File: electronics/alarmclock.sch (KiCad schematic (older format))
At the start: 31 parts, among them J1 Conn_01x02, J2 SWD, J3 SocketTop, J4 SocketBottom, J5 Conn_01x02, Q1 Backpower, SW1 Rotary_Encoder_Switch, SW2 Reset, U1 STM32L031F6P6, U2 74HC595, U3 74HC595, U4 AP2111H-3.3, Y1 24MHz

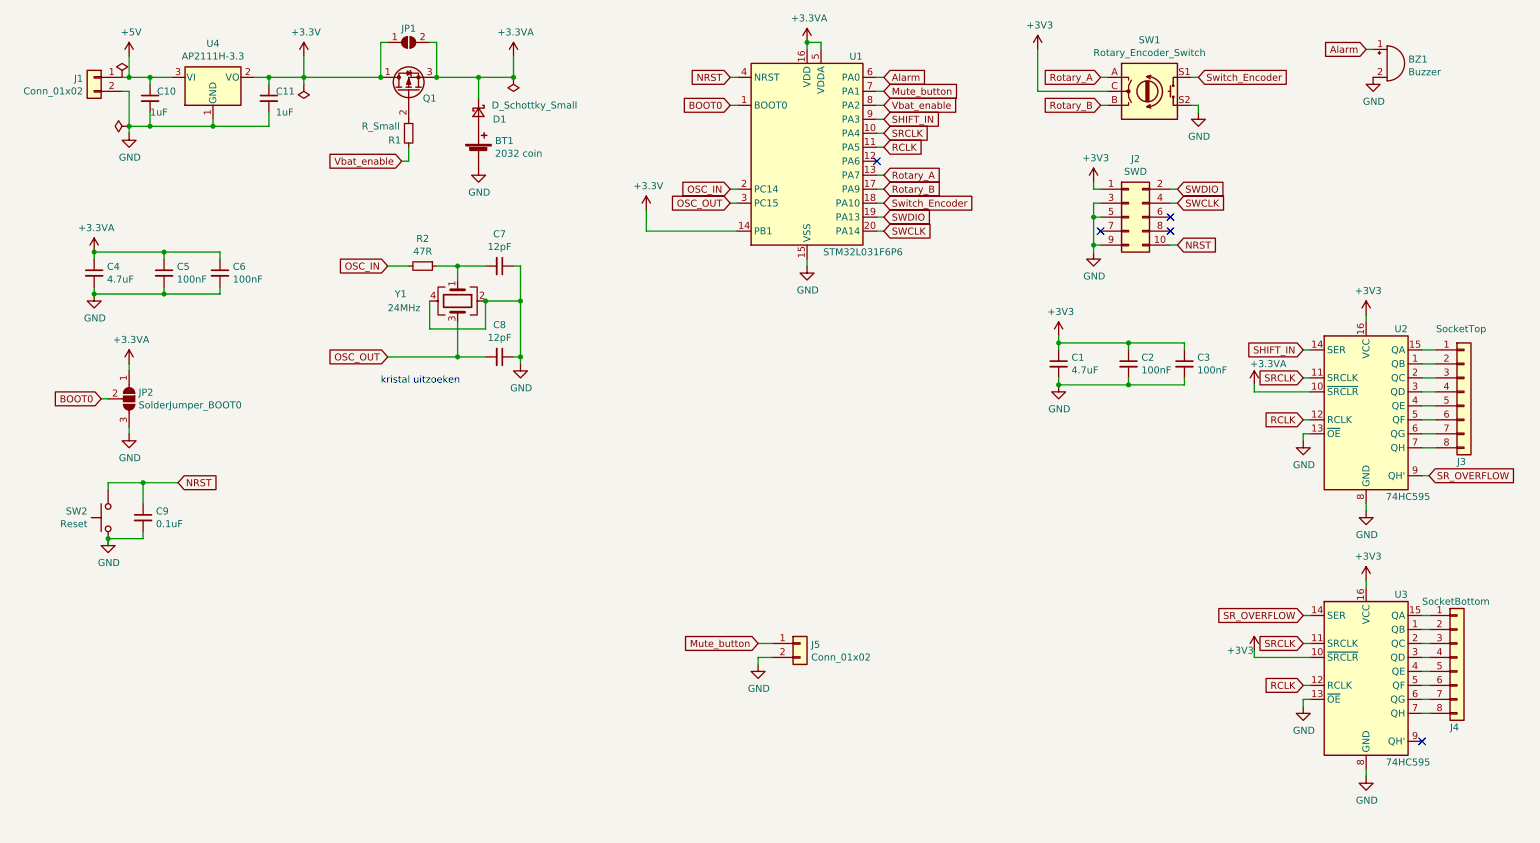
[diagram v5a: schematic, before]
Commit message: updated to kicad 7
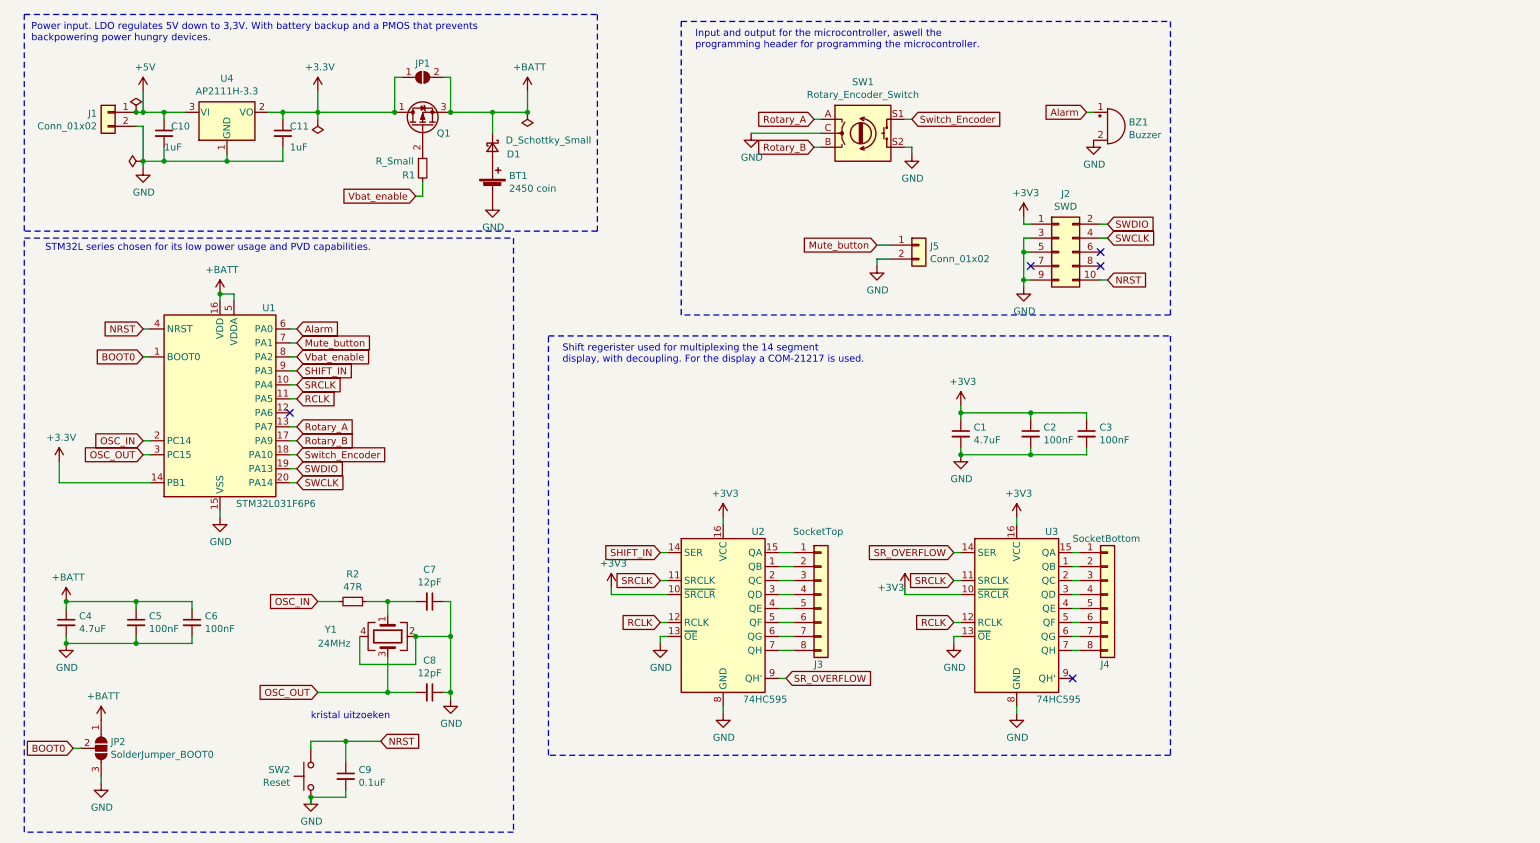
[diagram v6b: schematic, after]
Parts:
- BT1: value 2032 coin -> 2450 coin
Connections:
- net +3V3: now also U2.10 (~SRCLR); no longer SW1.C
- net GND: now also SW1.C
- net +3.3VA renamed +BATT
- net +BATT: no longer U2.10 (~SRCLR)
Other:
- note added: "Input and output for the microcontroller, aswell the \nprogramming header for programming the microcontroller.\n"
- note added: "Power input. LDO regulates 5V down to 3,3V. With battery backup and a PMOS that prevents \nbackpowering power hungry devices.\n"
- note added: "STM32L series chosen for its low power usage and PVD capabilities.\n"
- note added: "Shift regerister used for multiplexing the 14 segment\ndisplay, with decoupling. For the display a COM-21217 is used."
- moved on the sheet: BT1, BZ1, C1, C10, C11, C2, C3, C4, C5, C6, C7, C8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
